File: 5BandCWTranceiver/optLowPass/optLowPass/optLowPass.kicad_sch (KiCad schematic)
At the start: 74 parts, among them J1 Conn_01x06_Male, J2 Conn_01x02_Male, J3 Conn_Coaxial, J4 Conn_Coaxial, J5 Conn_01x02_Male, J6 Conn_01x02_Male, J7 Conn_01x02_Male, J8 Conn_01x02_Male, K1 G5V-2, K2 G5V-2, K3 G5V-2, K4 G5V-2, K5 G5V-2, Q1 MMBT3904, Q2 MMBT3904, Q3 MMBT3904, Q4 MMBT3904, Q5 MMBT3904

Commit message: First Tapeout
First tapeout of AptLowPass to JLCPCB
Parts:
- added C32: 628p, Capacitor_THT:C_Disc_D4.3mm_W1.9mm_P5.00mm, symbol Device:C
- added C33: 89p, Capacitor_THT:C_Disc_D4.3mm_W1.9mm_P5.00mm, symbol Device:C
- added C34: 1218p, Capacitor_THT:C_Disc_D4.3mm_W1.9mm_P5.00mm, symbol Device:C
- added C35: 202p, Capacitor_THT:C_Disc_D4.3mm_W1.9mm_P5.00mm, symbol Device:C
- added C36: 557p, Capacitor_THT:C_Disc_D4.3mm_W1.9mm_P5.00mm, symbol Device:C
- added C37: 435p, Capacitor_THT:C_Disc_D4.3mm_W1.9mm_P5.00mm, symbol Device:C
- added C38: 62p, Capacitor_THT:C_Disc_D4.3mm_W1.9mm_P5.00mm, symbol Device:C
- added C39: 844p, Capacitor_THT:C_Disc_D4.3mm_W1.9mm_P5.00mm, symbol Device:C
- added C40: 140p, Capacitor_THT:C_Disc_D4.3mm_W1.9mm_P5.00mm, symbol Device:C
- added C41: 386p, Capacitor_THT:C_Disc_D4.3mm_W1.9mm_P5.00mm, symbol Device:C
- added C42: 314p, Capacitor_THT:C_Disc_D4.3mm_W1.9mm_P5.00mm, symbol Device:C
- added C43: 44p, Capacitor_THT:C_Disc_D4.3mm_W1.9mm_P5.00mm, symbol Device:C
- added C44: 609p, Capacitor_THT:C_Disc_D4.3mm_W1.9mm_P5.00mm, symbol Device:C
- added C45: 101p, Capacitor_THT:C_Disc_D4.3mm_W1.9mm_P5.00mm, symbol Device:C
- added C46: 279p, Capacitor_THT:C_Disc_D4.3mm_W1.9mm_P5.00mm, symbol Device:C
- added C47: 244p, Capacitor_THT:C_Disc_D4.3mm_W1.9mm_P5.00mm, symbol Device:C
- added C48: 35p, Capacitor_THT:C_Disc_D4.3mm_W1.9mm_P5.00mm, symbol Device:C
- added C49: 474p, Capacitor_THT:C_Disc_D4.3mm_W1.9mm_P5.00mm, symbol Device:C
- added C50: 79p, Capacitor_THT:C_Disc_D4.3mm_W1.9mm_P5.00mm, symbol Device:C
- added C51: 217p, Capacitor_THT:C_Disc_D4.3mm_W1.9mm_P5.00mm, symbol Device:C
- added C52: 209p, Capacitor_THT:C_Disc_D4.3mm_W1.9mm_P5.00mm, symbol Device:C
- added C53: 30p, Capacitor_THT:C_Disc_D4.3mm_W1.9mm_P5.00mm, symbol Device:C
- added C54: 406p, Capacitor_THT:C_Disc_D4.3mm_W1.9mm_P5.00mm, symbol Device:C
- added C55: 67p, Capacitor_THT:C_Disc_D4.3mm_W1.9mm_P5.00mm, symbol Device:C
- added C56: 186p, Capacitor_THT:C_Disc_D4.3mm_W1.9mm_P5.00mm, symbol Device:C
- C10, C11, C12, C13, C14, C15, C16, C17, C18, C22, C23, C24, C25, C26, C27, C28, C29, C30, C31, C4, C5, C6, C7, C8, C9: footprint Library:C_Disc_DUAL_D4.3mm_W1.9mm_P5.00mm -> Capacitor_THT:C_Disc_D4.3mm_W1.9mm_P5.00mm
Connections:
- net GND: now also C32.2, C34.2, C36.2, C37.2, C39.2, C41.2, C42.2, C44.2, C46.2, C47.2, C49.2, C51.2, C52.2, C54.2, C56.2
- net at C12.2, C18.1, C9.1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: now also C43.1, C44.1, C45.2
- net at C11.1, C14.1, K2.13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: now also C40.1, C41.1
- net at C11.2, C17.1, C8.1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: now also C38.1, C39.1, C40.2
- net at C25.1, C27.2, C31.1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: now also C53.1, C54.1, C55.2
- net at C23.1, C31.2, K5.4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: now also C52.1, C53.2
- net at C12.1, C15.1, K3.13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: now also C45.1, C46.1
- net at C18.2, C6.1, K3.4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: now also C42.1, C43.2
- net at C10.1, C13.1, K1.13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: now also C35.1, C36.1
- net at C10.2, C16.1, C7.1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: now also C33.1, C34.1, C35.2
- net at C27.1, C29.1, K5.13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: now also C55.1, C56.1
- net at C17.2, C5.1, K2.4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: now also C37.1, C38.2
- net at C16.2, C4.1, K1.4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: now also C32.1, C33.2
- net at C22.1, C30.2, K4.4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: now also C47.1, C48.2
- net at C26.1, C28.1, K4.13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: now also C50.1, C51.1
- net at C24.1, C26.2, C30.1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: now also C48.1, C49.1, C50.2

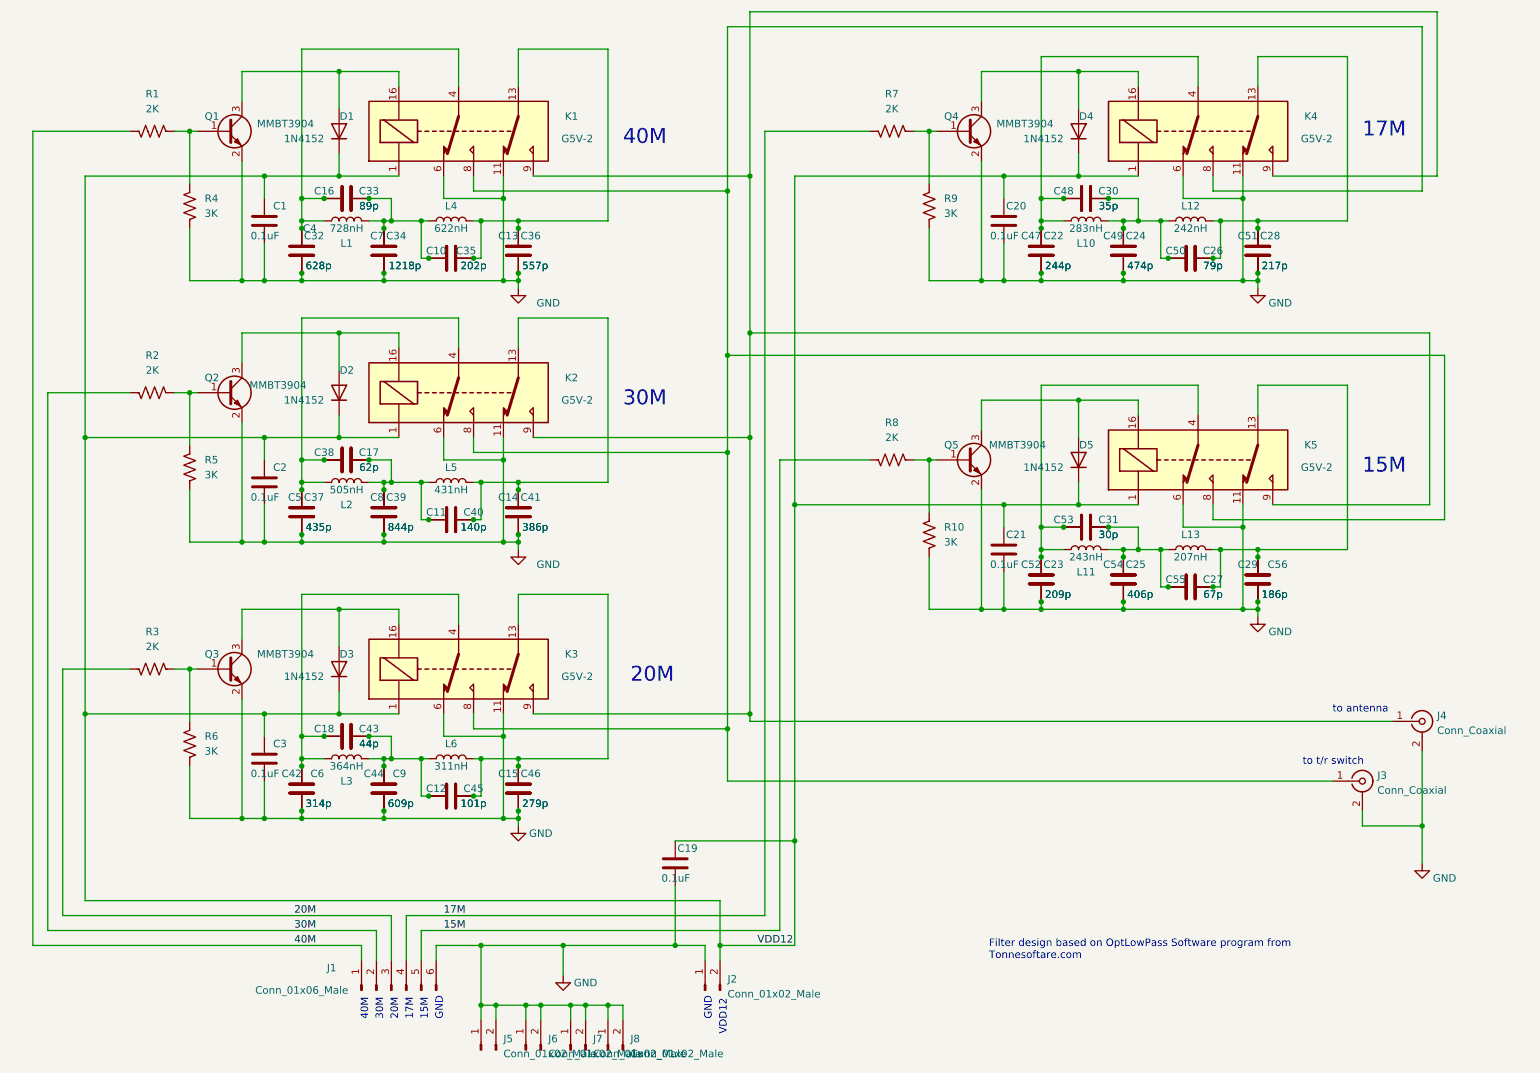
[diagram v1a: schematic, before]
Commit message: Updated OptLowPass schematic
Change to SMD caps and prepare for final layout
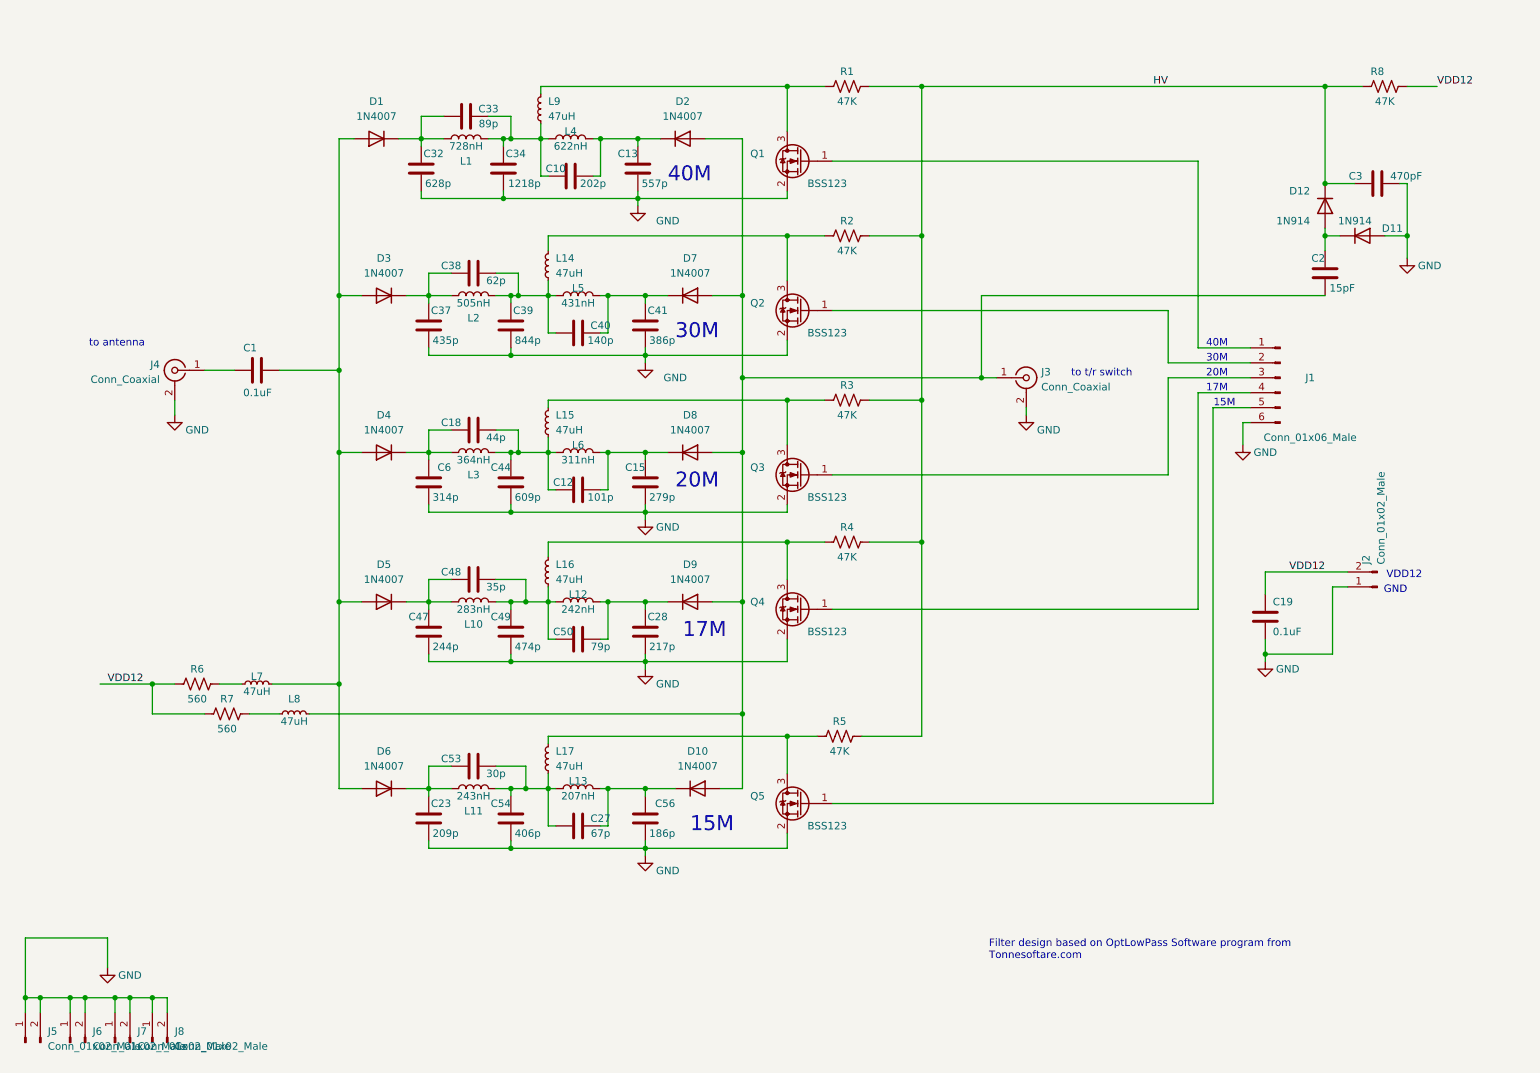
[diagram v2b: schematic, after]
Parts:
- removed C11: 140p, Capacitor_THT:C_Disc_D4.3mm_W1.9mm_P5.00mm, symbol Device:C
- removed C14: 386p, Capacitor_THT:C_Disc_D4.3mm_W1.9mm_P5.00mm, symbol Device:C
- removed C16: 89p, Capacitor_THT:C_Disc_D4.3mm_W1.9mm_P5.00mm, symbol Device:C
- removed C17: 62p, Capacitor_THT:C_Disc_D4.3mm_W1.9mm_P5.00mm, symbol Device:C
- removed C20, C21: 0.1uF, Capacitor_SMD:C_0603_1608Metric_Pad1.08x0.95mm_HandSolder, symbol Device:C
- removed C22: 244p, Capacitor_THT:C_Disc_D4.3mm_W1.9mm_P5.00mm, symbol Device:C
- removed C24: 474p, Capacitor_THT:C_Disc_D4.3mm_W1.9mm_P5.00mm, symbol Device:C
- removed C25: 406p, Capacitor_THT:C_Disc_D4.3mm_W1.9mm_P5.00mm, symbol Device:C
- removed C26: 79p, Capacitor_THT:C_Disc_D4.3mm_W1.9mm_P5.00mm, symbol Device:C
- removed C29: 186p, Capacitor_THT:C_Disc_D4.3mm_W1.9mm_P5.00mm, symbol Device:C
- removed C30: 35p, Capacitor_THT:C_Disc_D4.3mm_W1.9mm_P5.00mm, symbol Device:C
- removed C31: 30p, Capacitor_THT:C_Disc_D4.3mm_W1.9mm_P5.00mm, symbol Device:C
- removed C35: 202p, Capacitor_THT:C_Disc_D4.3mm_W1.9mm_P5.00mm, symbol Device:C
- removed C36: 557p, Capacitor_THT:C_Disc_D4.3mm_W1.9mm_P5.00mm, symbol Device:C
- removed C4: 628p, Capacitor_THT:C_Disc_D4.3mm_W1.9mm_P5.00mm, symbol Device:C
- removed C42: 314p, Capacitor_THT:C_Disc_D4.3mm_W1.9mm_P5.00mm, symbol Device:C
- removed C43: 44p, Capacitor_THT:C_Disc_D4.3mm_W1.9mm_P5.00mm, symbol Device:C
- removed C45: 101p, Capacitor_THT:C_Disc_D4.3mm_W1.9mm_P5.00mm, symbol Device:C
- removed C46: 279p, Capacitor_THT:C_Disc_D4.3mm_W1.9mm_P5.00mm, symbol Device:C
- removed C5: 435p, Capacitor_THT:C_Disc_D4.3mm_W1.9mm_P5.00mm, symbol Device:C
- removed C51: 217p, Capacitor_THT:C_Disc_D4.3mm_W1.9mm_P5.00mm, symbol Device:C
- removed C52: 209p, Capacitor_THT:C_Disc_D4.3mm_W1.9mm_P5.00mm, symbol Device:C
- removed C55: 67p, Capacitor_THT:C_Disc_D4.3mm_W1.9mm_P5.00mm, symbol Device:C
- removed C7: 1218p, Capacitor_THT:C_Disc_D4.3mm_W1.9mm_P5.00mm, symbol Device:C
- removed C8: 844p, Capacitor_THT:C_Disc_D4.3mm_W1.9mm_P5.00mm, symbol Device:C
- removed C9: 609p, Capacitor_THT:C_Disc_D4.3mm_W1.9mm_P5.00mm, symbol Device:C
- removed D1, D2, D3, D4, D5: 1N4152, Diode_THT:D_DO-41_SOD81_P7.62mm_Horizontal, symbol Device:D
- removed K1, K2, K3, K4, K5: G5V-2, Relay_THT:Relay_DPDT_Omron_G5V-2, symbol Relay:G5V-2
- removed Q1, Q2, Q3, Q4, Q5: MMBT3904, Package_TO_SOT_SMD:SOT-23, symbol Device:Q_NPN_BEC
- removed R10, R9: 3K, Resistor_SMD:R_0603_1608Metric_Pad0.98x0.95mm_HandSolder, symbol Device:R_US
- added D1, D10, D2, D3, D4, D5, D6, D7, D8, D9: 1N4007, Diode_THT:D_DO-41_SOD81_P10.16mm_Horizontal, symbol Diode:1N4007
- added D11, D12: 1N914, Diode_THT:D_DO-35_SOD27_P7.62mm_Horizontal, symbol Diode:1N914
- added L14, L15, L16, L17, L7, L8, L9: 47uH, Inductor_THT:L_Axial_L11.0mm_D4.5mm_P15.24mm_Horizontal_Fastron_MECC, symbol Device:L_Small
- added Q1, Q2, Q3, Q4, Q5: BSS123, Package_TO_SOT_SMD:SOT-23-3, symbol Device:Q_NMOS_GSD
- C1: footprint Capacitor_SMD:C_0603_1608Metric_Pad1.08x0.95mm_HandSolder -> Capacitor_THT:C_Disc_D4.3mm_W1.9mm_P5.00mm
- C10, C12, C13, C15, C18, C28, C32, C33, C34, C37, C38, C39, C40, C41, C44, C47, C48, C49, C50, C6: footprint Capacitor_THT:C_Disc_D4.3mm_W1.9mm_P5.00mm -> Capacitor_SMD:C_1206_3216Metric_Pad1.33x1.80mm_HandSolder
- C2: value 0.1uF -> 15pF; footprint Capacitor_SMD:C_0603_1608Metric_Pad1.08x0.95mm_HandSolder -> Capacitor_THT:C_Disc_D4.3mm_W1.9mm_P5.00mm
- C3: value 0.1uF -> 470pF; footprint Capacitor_SMD:C_0603_1608Metric_Pad1.08x0.95mm_HandSolder -> Capacitor_THT:C_Disc_D4.3mm_W1.9mm_P5.00mm
- R1, R2, R3, R8: value 2K -> 47K
- R4, R5: value 3K -> 47K
- R6: value 3K -> 560; footprint Resistor_SMD:R_0603_1608Metric_Pad0.98x0.95mm_HandSolder -> (none)
- R7: value 2K -> 560; footprint Resistor_SMD:R_0603_1608Metric_Pad0.98x0.95mm_HandSolder -> (none)
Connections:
- net GND: now also C19.1, D11.2 (A), Q1.2 (S), Q2.2 (S), Q3.2 (S), Q4.2 (S), Q5.2 (S); no longer C1.2, C19.2, C2.2, R4.2, R5.2, R6.2
- net VDD12: now also C19.2, R6.1, R7.1, R8.1; no longer C1.1, C19.1, C2.1, C3.1
- net at C12.2, C18.1, C44.1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: now also L15.1
- net at C40.1, C41.1, L5.1: now also D7.1 (K)
- net at C38.1, C39.1, C40.2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: now also L14.1
- net at R3.1: now also L15.2, Q3.3 (D); no longer R6.1
- net at C27.2, C53.1, C54.1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: now also L17.1
- net at C23.1, C53.2, L11.2: now also D6.1 (K)
- net at C12.1, C15.1, L6.1: now also D8.1 (K)
- net at C18.2, C6.1, L3.2: now also D4.1 (K)
- net at J3.1 (In): now also C2.2, D10.2 (A), D2.2 (A), D7.2 (A), D8.2 (A), D9.2 (A), L8.2
- net at J4.1 (In): now also C1.1
- net at C37.1, C38.2, L2.2: now also D3.1 (K)
- net at C27.1, C56.1, L13.1: now also D10.1 (K)
- net at C10.1, C13.1, L4.1: now also D2.1 (K)
- net at C10.2, C33.1, C34.1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: now also L9.1
- net at R4.1: now also L16.2, Q4.3 (D); no longer R1.1
- net at C32.1, C33.2, L1.2: now also D1.1 (K)
- net at C47.1, C48.2, L10.2: now also D5.1 (K)
- net at C28.1, C50.1, L12.1: now also D9.1 (K)
- net at R5.1: now also L17.2, Q5.3 (D); no longer R2.1
- net at C48.1, C49.1, C50.2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: now also L16.1
- net 15M: no longer names the net of J1.5 (Pin_5)
- net 15M: now also Q5.1 (G); no longer R8.2
- net 17M: no longer names the net of J1.4 (Pin_4)
- net 17M: now also Q4.1 (G); no longer R7.2
- net 20M: no longer names the net of J1.3 (Pin_3)
- net 20M: now also Q3.1 (G); no longer R3.2
- net 30M: no longer names the net of J1.2 (Pin_2)
- net 30M: now also Q2.1 (G); no longer R2.2
- net 40M: no longer names the net of J1.1 (Pin_1)
- net 40M: now also Q1.1 (G); no longer R1.2
- new net: C1.2, D1.2 (A), D3.2 (A), D4.2 (A), D5.2 (A), D6.2 (A), L7.2
- new net: L8.1, R7.2
- new net: C2.1, D11.1 (K), D12.2 (A)
- new net: L14.2, Q2.3 (D), R2.1
- new net: L9.2, Q1.3 (D), R1.1
- new net: L7.1, R6.2
- new net HV: C3.1, D12.1 (K), R1.2, R2.2, R3.2, R4.2, R5.2, R8.2
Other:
- moved on the sheet: C10, C12, C13, C15, C18, C19, C23, C27, C28, C32, C33, C34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

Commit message: Ready for tapeout
Filter board now with diode switching and SMD caps; power amp board updated with beefier dual nmos.
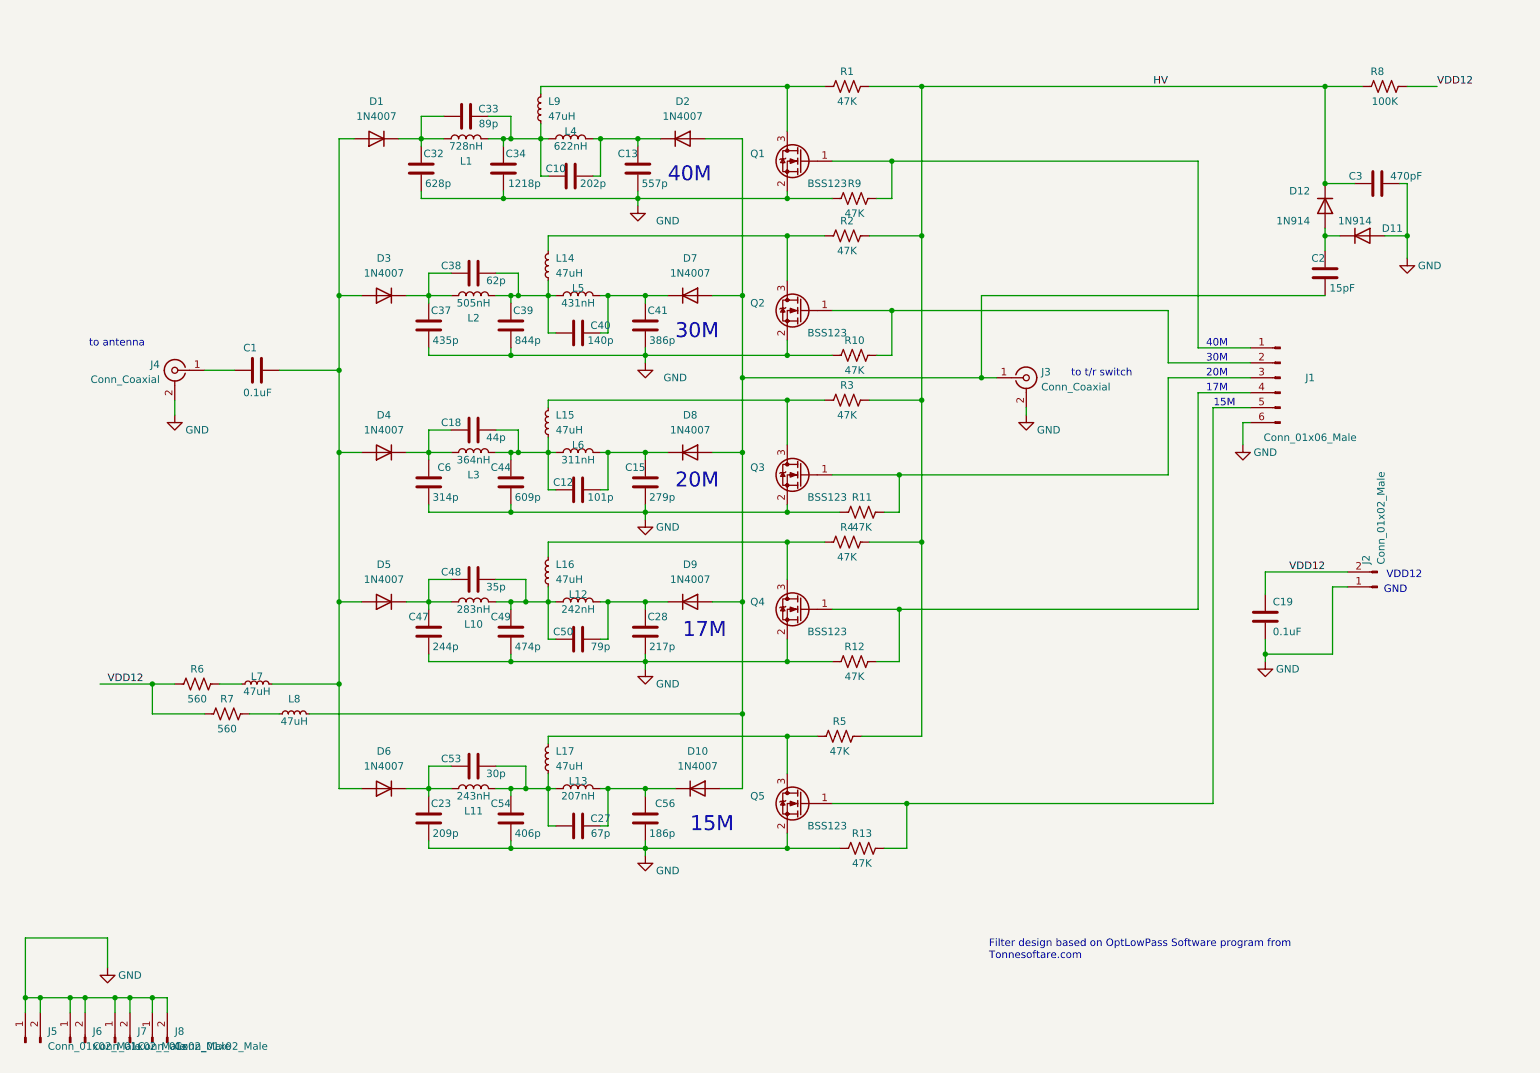
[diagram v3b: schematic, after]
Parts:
- added R10, R11, R12, R13, R9: 47K, Resistor_SMD:R_0603_1608Metric_Pad0.98x0.95mm_HandSolder, symbol Device:R_US
- C23, C27, C53, C54, C56: footprint Capacitor_THT:C_Disc_D4.3mm_W1.9mm_P5.00mm -> Capacitor_SMD:C_1206_3216Metric_Pad1.33x1.80mm_HandSolder
- L14, L15, L16, L17, L7, L8, L9: footprint Inductor_THT:L_Axial_L11.0mm_D4.5mm_P15.24mm_Horizontal_Fastron_MECC -> Inductor_THT:L_Axial_L11.0mm_D4.5mm_P7.62mm_Vertical_Fastron_MECC
- R6, R7: footprint (none) -> Resistor_THT:R_Axial_DIN0617_L17.0mm_D6.0mm_P20.32mm_Horizontal
- R8: value 47K -> 100K
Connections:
- net GND: now also R10.1, R11.1, R12.1, R13.1, R9.1
- net at J1.4 (Pin_4), Q4.1 (G): now also R12.2
- net at J1.3 (Pin_3), Q3.1 (G): now also R11.2
- net at J1.1 (Pin_1), Q1.1 (G): now also R9.2
- net at J1.5 (Pin_5), Q5.1 (G): now also R13.2
- net at J1.2 (Pin_2), Q2.1 (G): now also R10.2
